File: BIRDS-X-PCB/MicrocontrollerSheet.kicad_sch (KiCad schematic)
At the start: 1 part, among them U1 STM32G031K8Tx

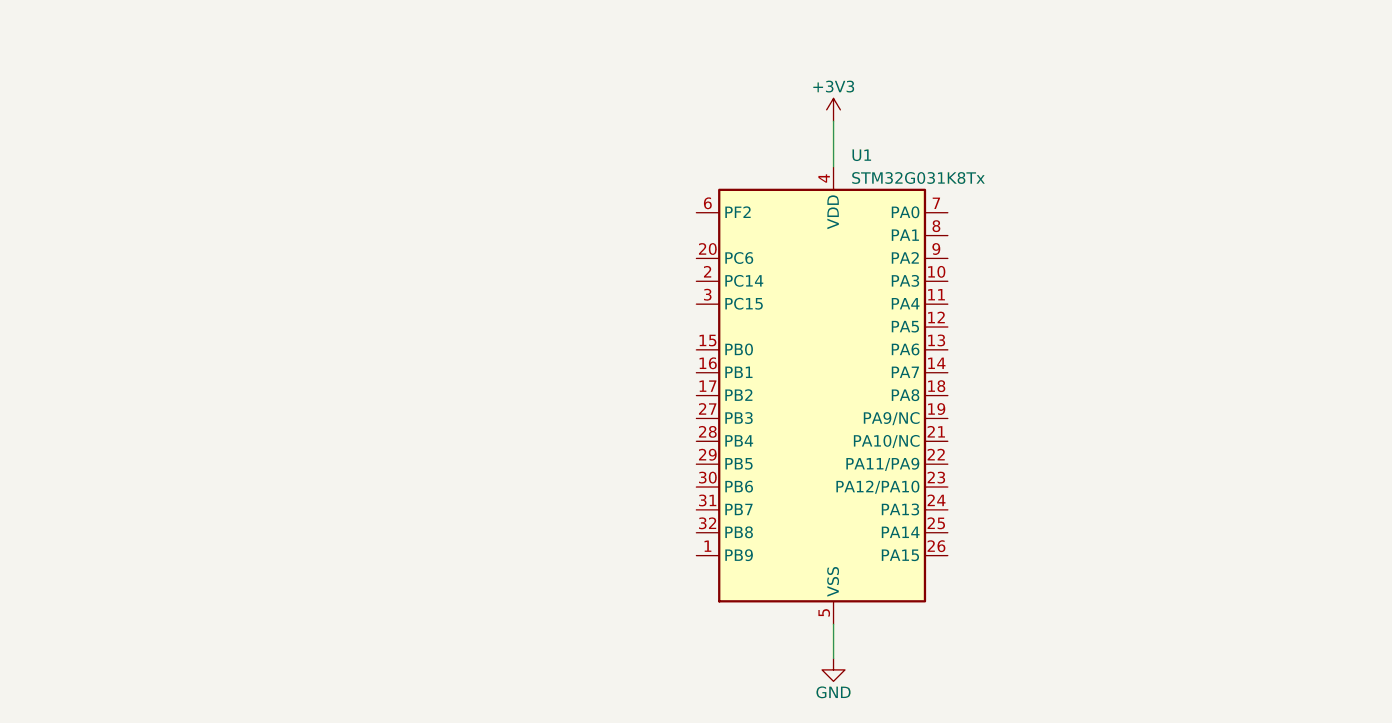
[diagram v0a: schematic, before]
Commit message: Added microcontroller circuitry
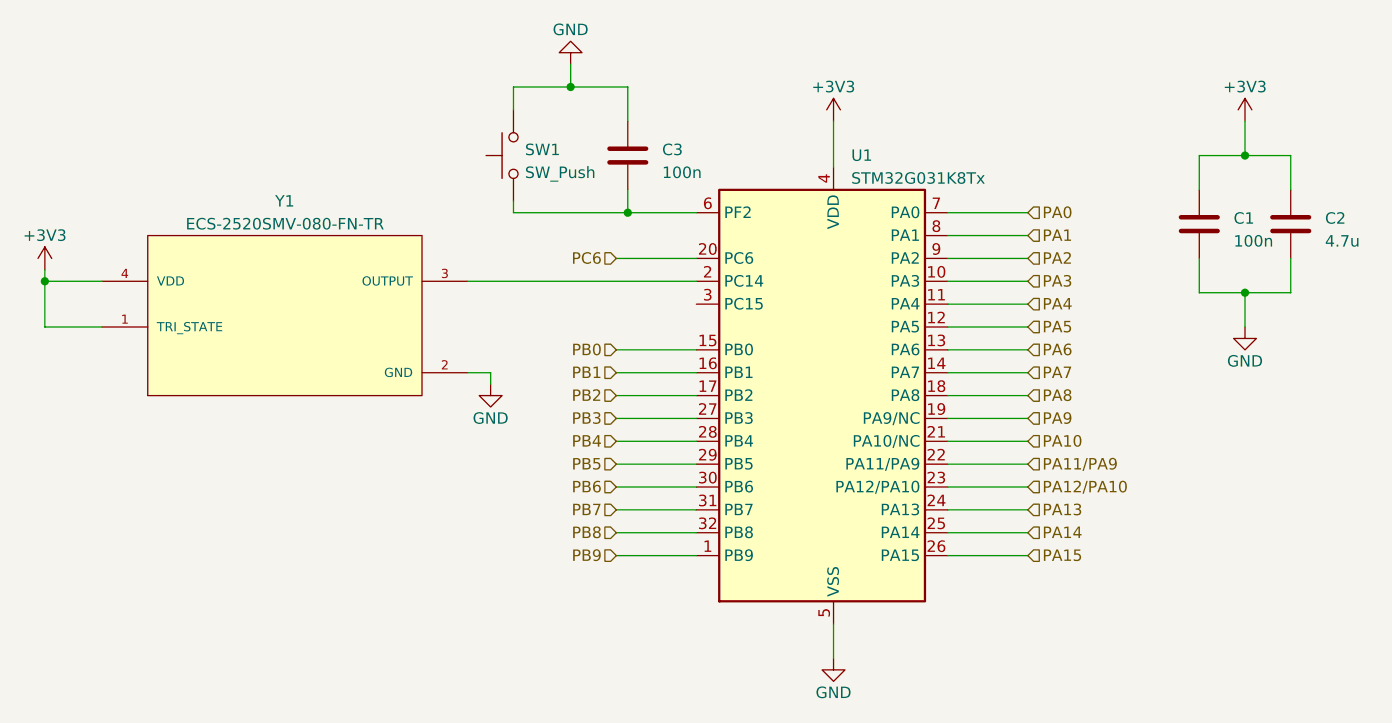
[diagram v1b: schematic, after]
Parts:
- added C1, C3: 100n, symbol Device:C
- added C2: 4.7u, symbol Device:C
- added SW1: SW_Push, symbol Switch:SW_Push
- added Y1: ECS-2520SMV-080-FN-TR, ECS-2520SMV-080-FN-TR:ECS-2520SMV-080-FN-TR, symbol ECS-2520SMV-080-FN-TR:ECS-2520SMV-080-FN-TR
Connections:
- net +3V3: now also C1.1, C2.1, Y1.1 (TRI_STATE), Y1.4 (VDD)
- net GND: now also C1.2, C2.2, C3.1, SW1.2, Y1.2 (GND)
- net PB9: now reaches U1.1 (PB9)
- net PA3: now reaches U1.10 (PA3)
- net PA4: now reaches U1.11 (PA4)
- net PA5: now reaches U1.12 (PA5)
- net PA6: now reaches U1.13 (PA6)
- net PA7: now reaches U1.14 (PA7)
- net PB0: now reaches U1.15 (PB0)
- net PB1: now reaches U1.16 (PB1)
- net PB2: now reaches U1.17 (PB2)
- net PA8: now reaches U1.18 (PA8)
- net PA9: now reaches U1.19 (PA9/NC)
- net at U1.2 (PC14): now also Y1.3 (OUTPUT)
- net PC6: now reaches U1.20 (PC6)
- net PA10: now reaches U1.21 (PA10/NC)
- net PA11/PA9: now reaches U1.22 (PA11/PA9)
- net PA12/PA10: now reaches U1.23 (PA12/PA10)
- net PA13: now reaches U1.24 (PA13)
- net PA14: now reaches U1.25 (PA14)
- net PA15: now reaches U1.26 (PA15)
- net PB3: now reaches U1.27 (PB3)
- net PB4: now reaches U1.28 (PB4)
- net PB5: now reaches U1.29 (PB5)
- net PB6: now reaches U1.30 (PB6)
- net PB7: now reaches U1.31 (PB7)
- net PB8: now reaches U1.32 (PB8)
- net at U1.6 (PF2): now also C3.2, SW1.1
- net PA0: now reaches U1.7 (PA0)
- net PA1: now reaches U1.8 (PA1)
- net PA2: now reaches U1.9 (PA2)

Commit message: Migrate libraries, create LTC4361 symbol
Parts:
- Y1: footprint ECS-2520SMV-080-FN-TR:ECS-2520SMV-080-FN-TR -> OSC_ECS-2520SMV-080-FN-TR
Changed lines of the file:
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@@
       (effects (font (size 1.27 1.27)))
     )
-    (property "Footprint" "ECS-2520SMV-080-FN-TR:ECS-2520SMV-080-FN-TR" (at 80.01 85.09 0)
+    (property "Footprint" "OSC_ECS-2520SMV-080-FN-TR" (at 80.01 85.09 0)
       (effects (font (size 1.27 1.27)) (justify bottom) hide)
     )

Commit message: Add more components
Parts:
- added U5: ~, symbol BIRDS-X_Symbols_Lib:MTT4B-Mini
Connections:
- net GND: now also U5.J2-1 (GND)
- net PB6: now also U5.J2-2 (PD0_UART_RX_EXT_TO_MTT4B)
- net PB7: now also U5.J2-4 (PD1_UART_TX_MTT4B_TO_EXT)
- new net +5V: U5.J2-3 (VCC)
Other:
- note added: "TODO add a 02x04 header to break out these pins"
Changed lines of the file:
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@@
 (kicad_sch (version 20230121) (generator eeschema)
   (paper "USLetter")
+  (junction (at 120.65 105.41) (diameter 0) (color 0 0 0 0)
+  )
   (junction (at 186.69 68.58) (diameter 0) (color 0 0 0 0)
   )
   (junction (at 111.76 60.96) (diameter 0) (color 0 0 0 0)
   )
+  (junction (at 123.19 107.95) (diameter 0) (color 0 0 0 0)
+  )
   (junction (at 186.69 83.82) (diameter 0) (color 0 0 0 0)
   )
@@
     (stroke (width 0) (type default))
   )
+  (wire (pts (xy 116.84 152.4) (xy 128.27 152.4))
+    (stroke (width 0) (type default))
+  )
   (wire (pts (xy 153.67 80.01) (xy 162.56 80.01))
     (stroke (width 0) (type default))
   )
+  (wire (pts (xy 123.19 107.95) (xy 125.73 107.95))
+    (stroke (width 0) (type default))
+  )
   (wire (pts (xy 102.87 92.71) (xy 102.87 93.98))
     (stroke (width 0) (type default))
@@
     (stroke (width 0) (type default))
   )
+  (wire (pts (xy 128.27 154.94) (xy 123.19 154.94))
+    (stroke (width 0) (type default))
+  )
+  (wire (pts (xy 116.84 110.49) (xy 125.73 110.49))
+    (stroke (width 0) (type default))
+  )
   (wire (pts (xy 186.69 68.58) (xy 191.77 68.58))
     (stroke (width 0) (type default))
@@
     (stroke (width 0) (type default))
   )
-  (wire (pts (xy 116.84 105.41) (xy 125.73 105.41))
+  (wire (pts (xy 120.65 149.86) (xy 120.65 105.41))
+    (stroke (width 0) (type default))
+  )
+  (wire (pts (xy 116.84 105.41) (xy 120.65 105.41))
+    (stroke (width 0) (type default))
+  )
+  (wire (pts (xy 123.19 107.95) (xy 123.19 154.94))
     (stroke (width 0) (type default))
   )
@@
     (stroke (width 0) (type default))
   )
+  (wire (pts (xy 119.38 147.32) (xy 128.27 147.32))
+    (stroke (width 0) (type default))
+  )
+  (wire (pts (xy 116.84 107.95) (xy 123.19 107.95))
+    (stroke (width 0) (type default))
+  )
   (wire (pts (xy 153.67 85.09) (xy 162.56 85.09))
     (stroke (width 0) (type default))
   )
+  (wire (pts (xy 120.65 105.41) (xy 125.73 105.41))
+    (stroke (width 0) (type default))
+  )
   (wire (pts (xy 105.41 63.5) (xy 105.41 60.96))
     (stroke (width 0) (type default))
   )
-  (wire (pts (xy 116.84 110.49) (xy 125.73 110.49))
-    (stroke (width 0) (type default))
-  )
   (wire (pts (xy 100.33 92.71) (xy 102.87 92.71))
     (stroke (width 0) (type default))
@@
     (stroke (width 0) (type default))
   )
-  (wire (pts (xy 116.84 107.95) (xy 125.73 107.95))
-    (stroke (width 0) (type default))
-  )
   (wire (pts (xy 153.67 77.47) (xy 162.56 77.47))
     (stroke (width 0) (type default))
@@
     (stroke (width 0) (type default))
   )
+  (wire (pts (xy 128.27 149.86) (xy 120.65 149.86))
+    (stroke (width 0) (type default))
+  )
   (wire (pts (xy 116.84 90.17) (xy 125.73 90.17))
     (stroke (width 0) (type default))
@@
     (stroke (width 0) (type default))
   )
+  (wire (pts (xy 119.38 147.32) (xy 119.38 160.02))
+    (stroke (width 0) (type default))
+  )
   (wire (pts (xy 118.11 74.93) (xy 118.11 72.39))
     (stroke (width 0) (type default))
@@
     (stroke (width 0) (type default))
   )
+  (wire (pts (xy 116.84 142.24) (xy 116.84 152.4))
+    (stroke (width 0) (type default))
+  )
   (wire (pts (xy 105.41 74.93) (xy 105.41 73.66))
     (stroke (width 0) (type default))
@@
   (wire (pts (xy 153.67 97.79) (xy 162.56 97.79))
     (stroke (width 0) (type default))
+  )
+  (text "TODO add a 02x04 header to break out these pins" (at 110.49 177.8 90)
+    (effects (font (size 1.27 1.27)) (justify left bottom))
   )
   (hierarchical_label "PC6" (shape input) (at 116.84 80.01 180) (fields_autoplaced)
@@
         (path "/c2796b15-795a-4d6e-ad4b-0ba87ded4bc9/d490f402-3a4d-40a5-b165-30c74c6560b7"
           (reference "#PWR03") (unit 1)
+        )
+      )
+    )
+  )
+  (symbol (lib_id "BIRDS-X_Symbols_Lib:MTT4B-Mini") (at 147.32 151.13 0) (unit 1)
+    (in_bom yes) (on_board yes) (dnp no) (fields_autoplaced)
+    (property "Reference" "U5" (at 163.83 151.765 0)
+      (effects (font (size 1.27 1.27)) (justify left))
+    )
+    (property "Value" "~" (at 144.78 157.48 0)
+      (effects (font (size 1.27 1.27)))
+    )
+    (property "Footprint" "" (at 144.78 157.48 0)
+      (effects (font (size 1.27 1.27)) hide)
+    )
+    (property "Datasheet" "" (at 144.78 157.48 0)
+      (effects (font (size 1.27 1.27)) hide)
+    )
+    (pin "J2-1")
+    (pin "J2-2")
+    (pin "J2-3")
+    (pin "J2-4")
+    (instances
+      (project "BIRDS-X-PCB"
+        (path "/c2796b15-795a-4d6e-ad4b-0ba87ded4bc9/d490f402-3a4d-40a5-b165-30c74c6560b7"
+          (reference "U5") (unit 1)
         )
       )
@@
     )
   )
+  (symbol (lib_id "power:GND") (at 119.38 160.02 0) (unit 1)
+    (in_bom yes) (on_board yes) (dnp no)
+    (property "Reference" "#PWR015" (at 119.38 166.37 0)
+      (effects (font (size 1.27 1.27)) hide)
+    )
+    (property "Value" "GND" (at 119.38 163.83 0)
+      (effects (font (size 1.27 1.27)))
+    )
+    (property "Footprint" "" (at 119.38 160.02 0)
+      (effects (font (size 1.27 1.27)) hide)
+    )
+    (property "Datasheet" "" (at 119.38 160.02 0)
+      (effects (font (size 1.27 1.27)) hide)
+    )
+    (pin "1")
+    (instances
+      (project "BIRDS-X-PCB"
+        (path "/c2796b15-795a-4d6e-ad4b-0ba87ded4bc9/d490f402-3a4d-40a5-b165-30c74c6560b7"
+          (reference "#PWR015") (unit 1)
+        )
+      )
+    )
+  )
   (symbol (lib_id "ECS-2520SMV-080-FN-TR:ECS-2520SMV-080-FN-TR") (at 80.01 85.09 0) (unit 1)
     (in_bom yes) (on_board yes) (dnp no) (fields_autoplaced)
@@
         )
       )
+    )
+  )
+  (symbol (lib_id "power:+5V") (at 116.84 142.24 0) (unit 1)
+    (in_bom yes) (on_board yes) (dnp no) (fields_autoplaced)
+    (property "Reference" "#PWR016" (at 116.84 146.05 0)
+      (effects (font (size 1.27 1.27)) hide)
+    )
+    (property "Value" "+5V" (at 116.84 138.43 0)
+      (effects (font (size 1.27 1.27)))
+    )
+    (property "Footprint" "" (at 116.84 142.24 0)
+      (effects (font (size 1.27 1.27)) hide)
+    )
+    (property "Datasheet" "" (at 116.84 142.24 0)
+      (effects (font (size 1.27 1.27)) hide)
+    )
+    (pin "1")
+    (instances
+      (project "BIRDS-X-PCB"
+        (path "/c2796b15-795a-4d6e-ad4b-0ba87ded4bc9/d490f402-3a4d-40a5-b165-30c74c6560b7"
+          (reference "#PWR016") (unit 1)
+        )
+      )

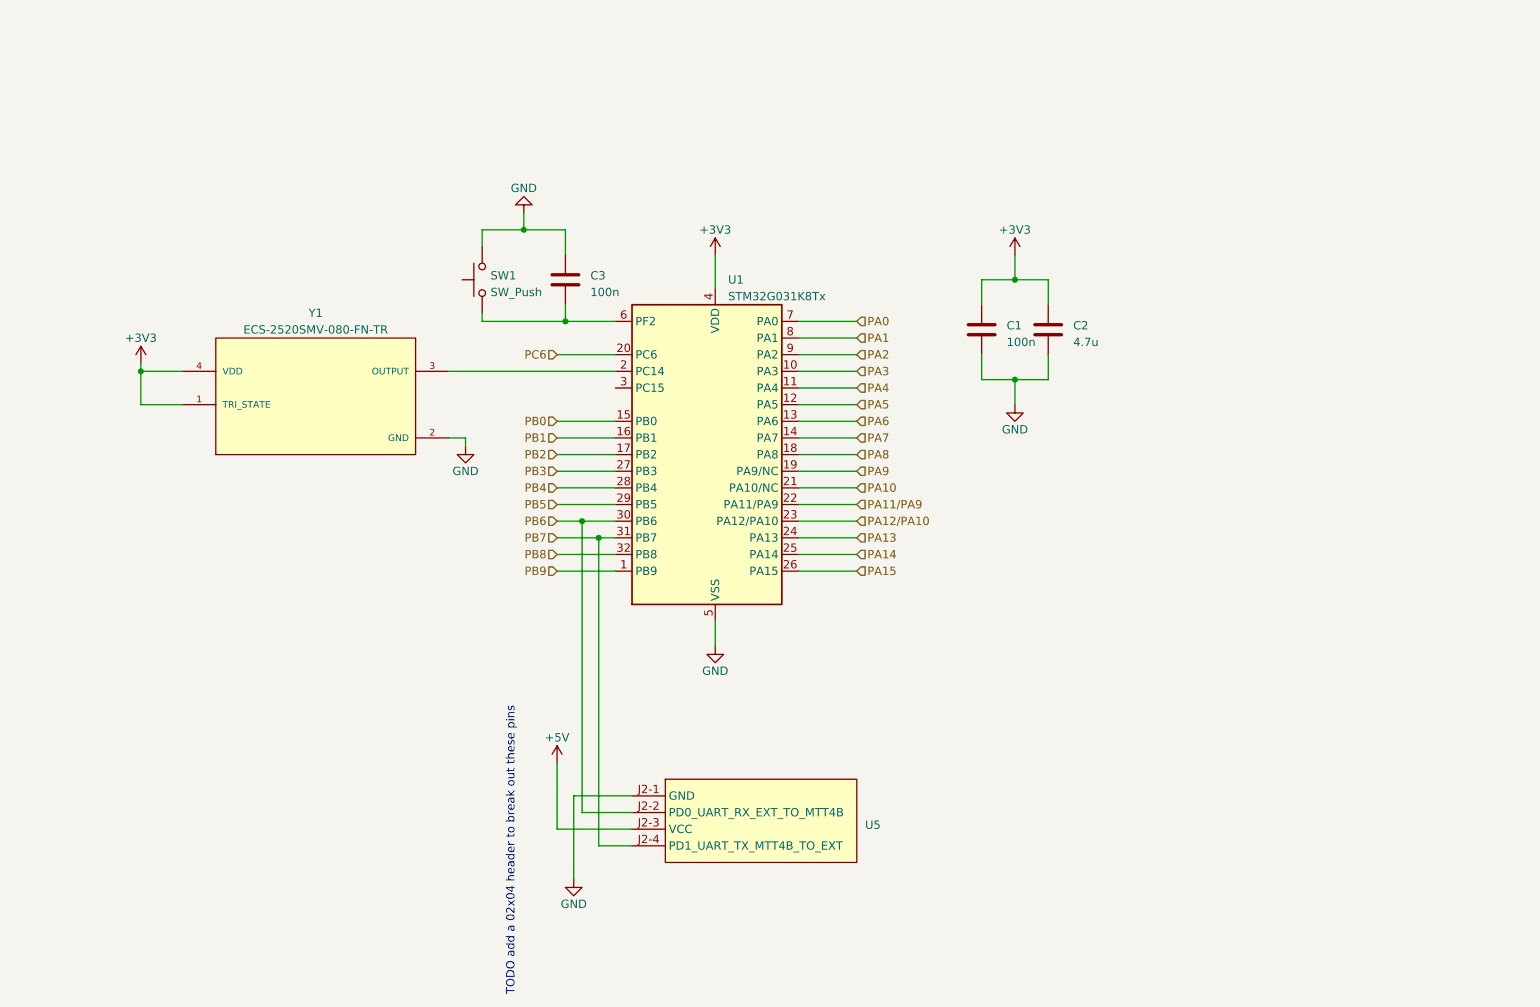
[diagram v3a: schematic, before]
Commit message: Add flash, temperature sensor, etc.
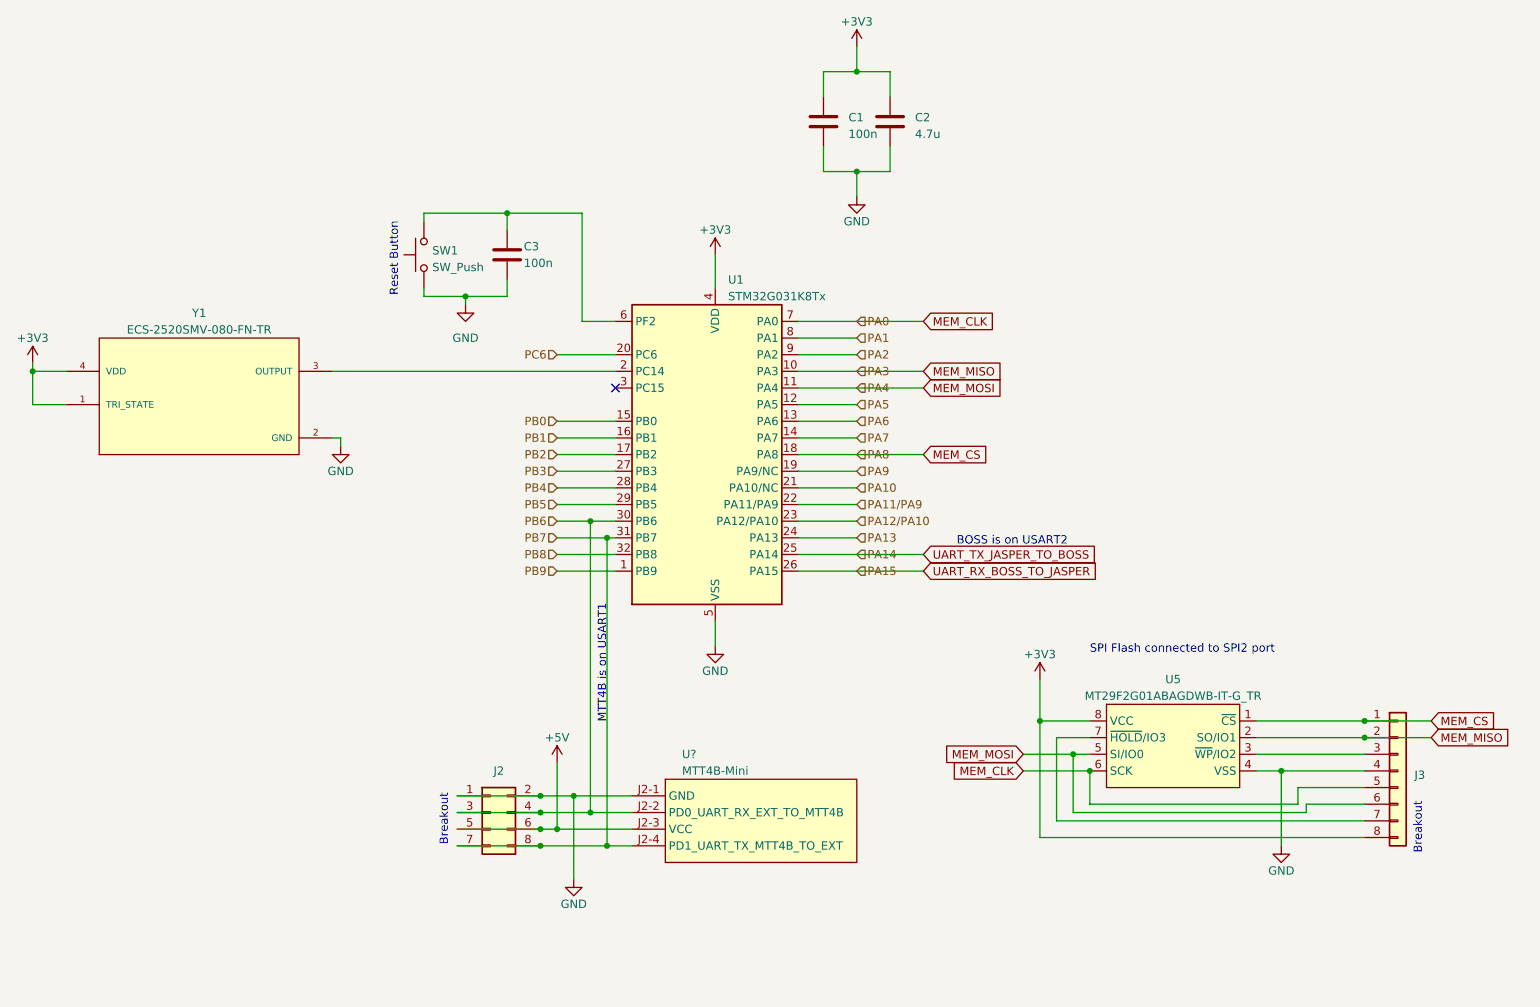
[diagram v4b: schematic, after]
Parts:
- added J2: Conn_02x04_Odd_Even, symbol Connector_Generic:Conn_02x04_Odd_Even
- added J3: Conn_01x08, symbol Connector_Generic:Conn_01x08
- added U5: MT29F2G01ABAGDWB-IT-G_TR, symbol BIRDS-X_Symbols_Lib:MT29F2G01ABAGDWB-IT-G_TR
- U?: renamed from U5; value ~ -> MTT4B-Mini
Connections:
- net +3V3: now also J3.8 (Pin_8), U5.8 (VCC)
- net +5V: now also J2.5 (Pin_5), J2.6 (Pin_6)
- net GND: now also C3.2, SW1.1, J2.1 (Pin_1), J2.2 (Pin_2), J3.4 (Pin_4), U5.4 (VSS); no longer C3.1, SW1.2
- net PB6: now also J2.3 (Pin_3), J2.4 (Pin_4)
- net PB7: now also J2.7 (Pin_7), J2.8 (Pin_8)
- net PA0 renamed MEM_CLK
- net MEM_CLK: now also J3.5 (Pin_5), U5.6 (SCK)
- net PA14 renamed UART_TX_JASPER_TO_BOSS
- net PA15 renamed UART_RX_BOSS_TO_JASPER
- net PA3 renamed MEM_MISO
- net MEM_MISO: now also J3.2 (Pin_2), U5.2 (SO/IO1)
- net PA4 renamed MEM_MOSI
- net MEM_MOSI: now also J3.6 (Pin_6), U5.5 (SI/IO0)
- net PA8 renamed MEM_CS
- net MEM_CS: now also J3.1 (Pin_1), U5.1 (~{CS})
- new net: J3.3 (Pin_3), U5.3 (~{WP}/IO2)
- new net: J3.7 (Pin_7), U5.7 (~{HOLD}/IO3)
- new net: C3.1, SW1.2, U1.6 (PF2)
- no-connect marks 0 -> 1
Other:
- note added: "BOSS is on USART2"
- note added: "Breakout"
- note added: "MTT4B is on USART1"
- note added: "Reset Button"
- note added: "SPI Flash connected to SPI2 port"
- note removed: "TODO add a 02x04 header to break out these pins"
- moved on the sheet: C1, C2, C3, SW1, Y1

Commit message: Add BOM and footprints
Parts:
- C401: renamed from C3; footprint (none) -> Capacitor_SMD:C_1206_3216Metric_Pad1.33x1.80mm_HandSolder
- C402: renamed from C1; footprint (none) -> Capacitor_SMD:C_1206_3216Metric_Pad1.33x1.80mm_HandSolder
- C403: renamed from C2; footprint (none) -> Capacitor_SMD:C_1206_3216Metric_Pad1.33x1.80mm_HandSolder
- J401: renamed from J2; footprint (none) -> Connector_PinSocket_2.54mm:PinSocket_2x04_P2.54mm_Vertical
- J402: renamed from J3; footprint (none) -> Connector_PinSocket_2.54mm:PinSocket_1x08_P2.54mm_Vertical
- SW401: renamed from SW1; footprint (none) -> Button_Switch_SMD:SW_SPST_EVPBF
- Y401: renamed from Y1; footprint OSC_ECS-2520SMV-080-FN-TR -> lib:OSC_ECS-2520SMV-080-FN-TR
- gave numbers to parts that had none: 1
- renumbered U1 to U401, U5 to U403
